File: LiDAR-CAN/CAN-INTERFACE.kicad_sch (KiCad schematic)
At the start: 19 parts, among them U4 TCAN4550RGY, Y2 40MHz

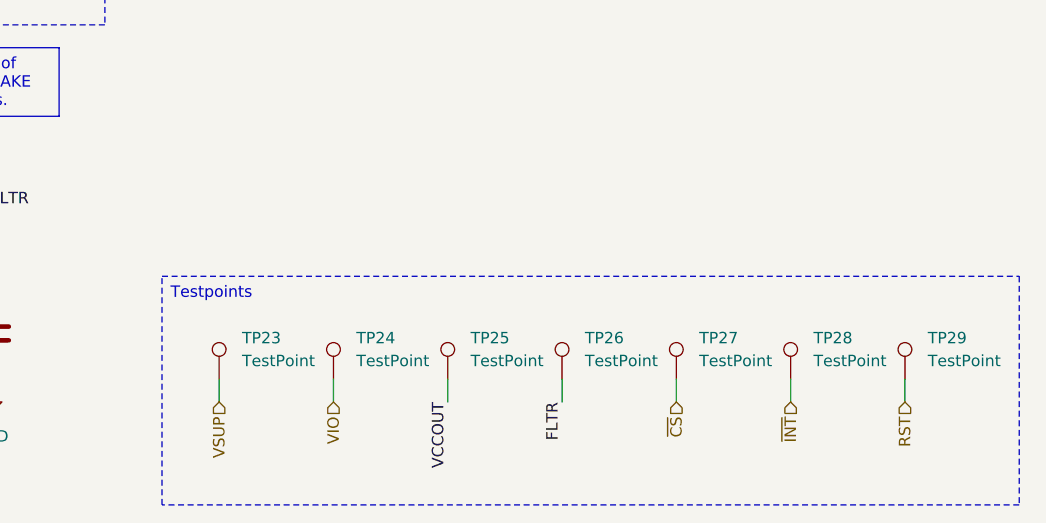
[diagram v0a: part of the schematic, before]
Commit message: Add SPI buses routing
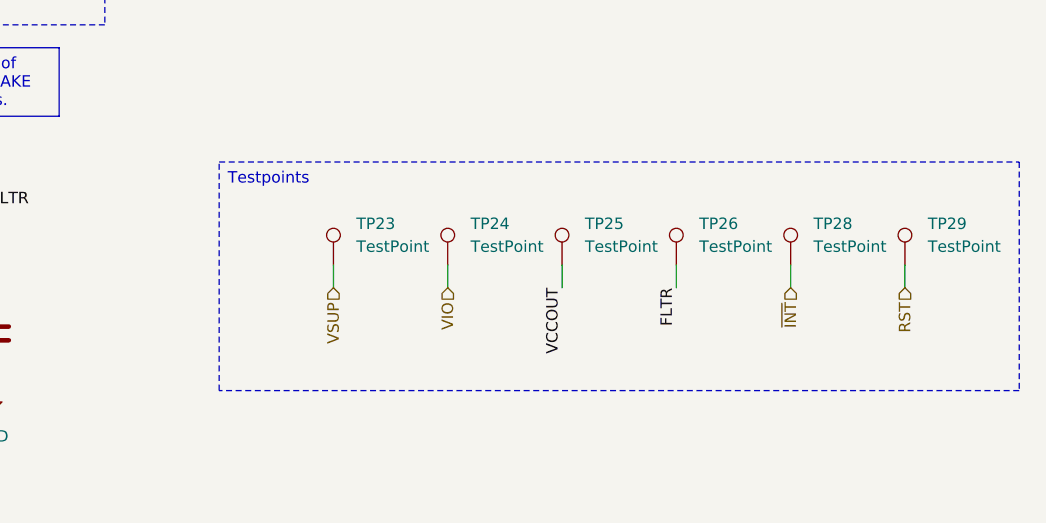
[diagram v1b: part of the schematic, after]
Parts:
- removed TP27: TestPoint, TestPoint:TestPoint_Pad_D1.0mm, symbol Connector:TestPoint
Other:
- moved on the sheet: TP23, TP24, TP25, TP26, TP28, TP29
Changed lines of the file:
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@@
 	(text_box "Testpoints"
 		(exclude_from_sim no)
-		(at 184.15 139.7 0)
-		(size 95.25 25.4)
+		(at 190.5 127 0)
+		(size 88.9 25.4)
 		(margins 0.9525 0.9525 0.9525 0.9525)
 		(stroke
@@
 	(wire
 		(pts
-			(xy 241.3 151.13) (xy 241.3 153.67)
-		)
-		(stroke
-			(width 0)
-			(type default)
-		)
-	)
-	(wire
-		(pts
 			(xy 165.1 142.24) (xy 165.1 132.08)
 		)
@@
 	(wire
 		(pts
-			(xy 215.9 151.13) (xy 215.9 153.67)
+			(xy 228.6 138.43) (xy 228.6 140.97)
 		)
 		(stroke
@@
 	(wire
 		(pts
-			(xy 190.5 151.13) (xy 190.5 153.67)
+			(xy 203.2 138.43) (xy 203.2 140.97)
 		)
 		(stroke
@@
 	(wire
 		(pts
-			(xy 203.2 151.13) (xy 203.2 153.67)
+			(xy 215.9 138.43) (xy 215.9 140.97)
 		)
 		(stroke
@@
 	(wire
 		(pts
-			(xy 254 151.13) (xy 254 153.67)
+			(xy 254 138.43) (xy 254 140.97)
 		)
 		(stroke
@@
 	(wire
 		(pts
-			(xy 266.7 151.13) (xy 266.7 153.67)
+			(xy 266.7 138.43) (xy 266.7 140.97)
 		)
 		(stroke
@@
 	(wire
 		(pts
-			(xy 228.6 151.13) (xy 228.6 153.67)
+			(xy 241.3 138.43) (xy 241.3 140.97)
 		)
 		(stroke
@@
 	)
 	(label "VCCOUT"
-		(at 215.9 153.67 270)
+		(at 228.6 140.97 270)
 		(effects
 			(font
@@
 	)
 	(label "FLTR"
-		(at 228.6 153.67 270)
+		(at 241.3 140.97 270)
 		(effects
 			(font
@@
 	(hierarchical_label "VIO"
 		(shape input)
-		(at 203.2 153.67 270)
+		(at 215.9 140.97 270)
 		(effects
 			(font
@@
 	(hierarchical_label "RST"
 		(shape input)
-		(at 266.7 153.67 270)
+		(at 266.7 140.97 270)
 		(effects
 			(font
@@
 	(hierarchical_label "~{INT}"
 		(shape input)
-		(at 254 153.67 270)
+		(at 254 140.97 270)
 		(effects
 			(font
@@
 	(hierarchical_label "VSUP"
 		(shape input)
-		(at 190.5 153.67 270)
+		(at 203.2 140.97 270)
 		(effects
 			(font
@@
 		)
 	)
-	(hierarchical_label "~{CS}"
-		(shape input)
-		(at 241.3 153.67 270)
-		(effects
-			(font
-				(size 1.27 1.27)
-			)
-			(justify right)
-		)
-	)
 	(hierarchical_label "SDO"
 		(shape output)
@@
 	(symbol
 		(lib_id "Connector:TestPoint")
-		(at 228.6 151.13 0)
+		(at 241.3 138.43 0)
 		(unit 1)
 		(exclude_from_sim no)
@@
 		(fields_autoplaced yes)
 		(property "Reference" "TP26"
-			(at 231.14 146.5579 0)
+			(at 243.84 133.8579 0)
 			(effects
 				(font
@@
 		)
 		(property "Value" "TestPoint"
-			(at 231.14 149.0979 0)
+			(at 243.84 136.3979 0)
 			(effects
 				(font
@@
 		)
 		(property "Footprint" "TestPoint:TestPoint_Pad_D1.0mm"
-			(at 233.68 151.13 0)
+			(at 246.38 138.43 0)
 			(effects
 				(font
@@
 		)
 		(property "Datasheet" "~"
-			(at 233.68 151.13 0)
+			(at 246.38 138.43 0)
 			(effects
 				(font
@@
 		)
 		(property "Description" "test point"
-			(at 228.6 151.13 0)
+			(at 241.3 138.43 0)
 			(effects
 				(font
@@
 	(symbol
 		(lib_id "Connector:TestPoint")
-		(at 190.5 151.13 0)
+		(at 203.2 138.43 0)
 		(unit 1)
 		(exclude_from_sim no)
@@
 		(fields_autoplaced yes)
 		(property "Reference" "TP23"
-			(at 193.04 146.5579 0)
+			(at 205.74 133.8579 0)
 			(effects
 				(font
@@
 		)
 		(property "Value" "TestPoint"
-			(at 193.04 149.0979 0)
+			(at 205.74 136.3979 0)
 			(effects
 				(font
@@
 		)
 		(property "Footprint" "TestPoint:TestPoint_Pad_D1.0mm"
-			(at 195.58 151.13 0)
+			(at 208.28 138.43 0)
 			(effects
 				(font
@@
 		)
 		(property "Datasheet" "~"
-			(at 195.58 151.13 0)
+			(at 208.28 138.43 0)
 			(effects
 				(font
@@
 		)
 		(property "Description" "test point"
-			(at 190.5 151.13 0)
+			(at 203.2 138.43 0)
 			(effects
 				(font
@@
 	)
 	(symbol
-		(lib_id "Connector:TestPoint")
-		(at 241.3 151.13 0)
-		(unit 1)
-		(exclude_from_sim no)
-		(in_bom no)
-		(on_board yes)
-		(dnp no)
-		(fields_autoplaced yes)
-		(property "Reference" "TP27"
-			(at 243.84 146.5579 0)
-			(effects
-				(font
-					(size 1.27 1.27)
-				)
-				(justify left)
-			)
-		)
-		(property "Value" "TestPoint"
-			(at 243.84 149.0979 0)
-			(effects
-				(font
-					(size 1.27 1.27)
-				)
-				(justify left)
-			)
-		)
-		(property "Footprint" "TestPoint:TestPoint_Pad_D1.0mm"
-			(at 246.38 151.13 0)
-			(effects
-				(font
-					(size 1.27 1.27)
-				)
-				(hide yes)
-			)
-		)
-		(property "Datasheet" "~"
-			(at 246.38 151.13 0)
-			(effects
-				(font
-					(size 1.27 1.27)
-				)
-				(hide yes)
-			)
-		)
-		(property "Description" "test point"
-			(at 241.3 151.13 0)
-			(effects
-				(font
-					(size 1.27 1.27)
-				)
-				(hide yes)
-			)
-		)
-		(pin "1"
-		)
-		(instances
-			(project "LiDAR-CAN"
-				(path "/56db6f21-0e4a-4321-bd8a-db37f1842dd9/acdb1e38-683e-41e3-b904-0eede9d7599d"
-					(reference "TP27")
-					(unit 1)
-				)
-			)
-		)
-	)
-	(symbol
 		(lib_id "Device:R_US")
 		(at 95.25 101.6 0)
@@
 	(symbol
 		(lib_id "Connector:TestPoint")
-		(at 254 151.13 0)
+		(at 254 138.43 0)
 		(unit 1)
 		(exclude_from_sim no)
@@
 		(fields_autoplaced yes)
 		(property "Reference" "TP28"
-			(at 256.54 146.5579 0)
+			(at 256.54 133.8579 0)
 			(effects
 				(font
@@
 		)
 		(property "Value" "TestPoint"
-			(at 256.54 149.0979 0)
+			(at 256.54 136.3979 0)
 			(effects
 				(font
@@
 		)
 		(property "Footprint" "TestPoint:TestPoint_Pad_D1.0mm"
-			(at 259.08 151.13 0)
+			(at 259.08 138.43 0)
 			(effects
 				(font
@@
 		)
 		(property "Datasheet" "~"
-			(at 259.08 151.13 0)
+			(at 259.08 138.43 0)
 			(effects
 				(font
@@
 		)
 		(property "Description" "test point"
-			(at 254 151.13 0)
+			(at 254 138.43 0)
 			(effects
 				(font
@@
 	(symbol
 		(lib_id "Connector:TestPoint")
-		(at 266.7 151.13 0)
+		(at 266.7 138.43 0)
 		(unit 1)
 		(exclude_from_sim no)
@@
 		(fields_autoplaced yes)
 		(property "Reference" "TP29"
-			(at 269.24 146.5579 0)
+			(at 269.24 133.8579 0)
 			(effects
 				(font
@@
 		)
 		(property "Value" "TestPoint"
-			(at 269.24 149.0979 0)
+			(at 269.24 136.3979 0)
 			(effects
 				(font
@@
 		)
 		(property "Footprint" "TestPoint:TestPoint_Pad_D1.0mm"
-			(at 271.78 151.13 0)
+			(at 271.78 138.43 0)
 			(effects
 				(font
@@
 		)
 		(property "Datasheet" "~"
-			(at 271.78 151.13 0)
+			(at 271.78 138.43 0)
 			(effects
 				(font
@@
 		)
 		(property "Description" "test point"
-			(at 266.7 151.13 0)
+			(at 266.7 138.43 0)
 			(effects
 				(font
@@
 	(symbol
 		(lib_id "Connector:TestPoint")
-		(at 203.2 151.13 0)
+		(at 215.9 138.43 0)
 		(unit 1)
 		(exclude_from_sim no)
@@
 		(fields_autoplaced yes)
 		(property "Reference" "TP24"
-			(at 205.74 146.5579 0)
+			(at 218.44 133.8579 0)
 			(effects
 				(font
@@
 		)
 		(property "Value" "TestPoint"
-			(at 205.74 149.0979 0)
+			(at 218.44 136.3979 0)
 			(effects
 				(font
@@
 		)
 		(property "Footprint" "TestPoint:TestPoint_Pad_D1.0mm"
-			(at 208.28 151.13 0)
+			(at 220.98 138.43 0)
 			(effects
 				(font
@@
 		)
 		(property "Datasheet" "~"
-			(at 208.28 151.13 0)
+			(at 220.98 138.43 0)
 			(effects
 				(font
@@
 		)
 		(property "Description" "test point"
-			(at 203.2 151.13 0)
+			(at 215.9 138.43 0)
 			(effects
 				(font
@@
 	(symbol
 		(lib_id "Connector:TestPoint")
-		(at 215.9 151.13 0)
+		(at 228.6 138.43 0)
 		(unit 1)
 		(exclude_from_sim no)
@@
 		(fields_autoplaced yes)
 		(property "Reference" "TP25"
-			(at 218.44 146.5579 0)
+			(at 231.14 133.8579 0)
 			(effects
 				(font
@@
 		)
 		(property "Value" "TestPoint"
-			(at 218.44 149.0979 0)
+			(at 231.14 136.3979 0)
 			(effects
 				(font
@@
 		)
 		(property "Footprint" "TestPoint:TestPoint_Pad_D1.0mm"
-			(at 220.98 151.13 0)
+			(at 233.68 138.43 0)
 			(effects
 				(font
@@
 		)
 		(property "Datasheet" "~"
-			(at 220.98 151.13 0)
+			(at 233.68 138.43 0)
 			(effects
 				(font
@@
 		)
 		(property "Description" "test point"
-			(at 215.9 151.13 0)
+			(at 228.6 138.43 0)
 			(effects
 				(font
